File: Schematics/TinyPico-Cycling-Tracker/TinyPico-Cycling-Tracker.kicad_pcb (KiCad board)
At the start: 2 copper layers, 105.2 x 70.1 mm, 17 parts, among them J1 Conn_01x06, J4 Conn_01x06_Socket, SW2 SW_Push, U10 MicroSD Card Adapter, U6 module_mpu6050, U7 SSD1306 0.96" OLED, U8 TinyPico, U9 GPS6MV2

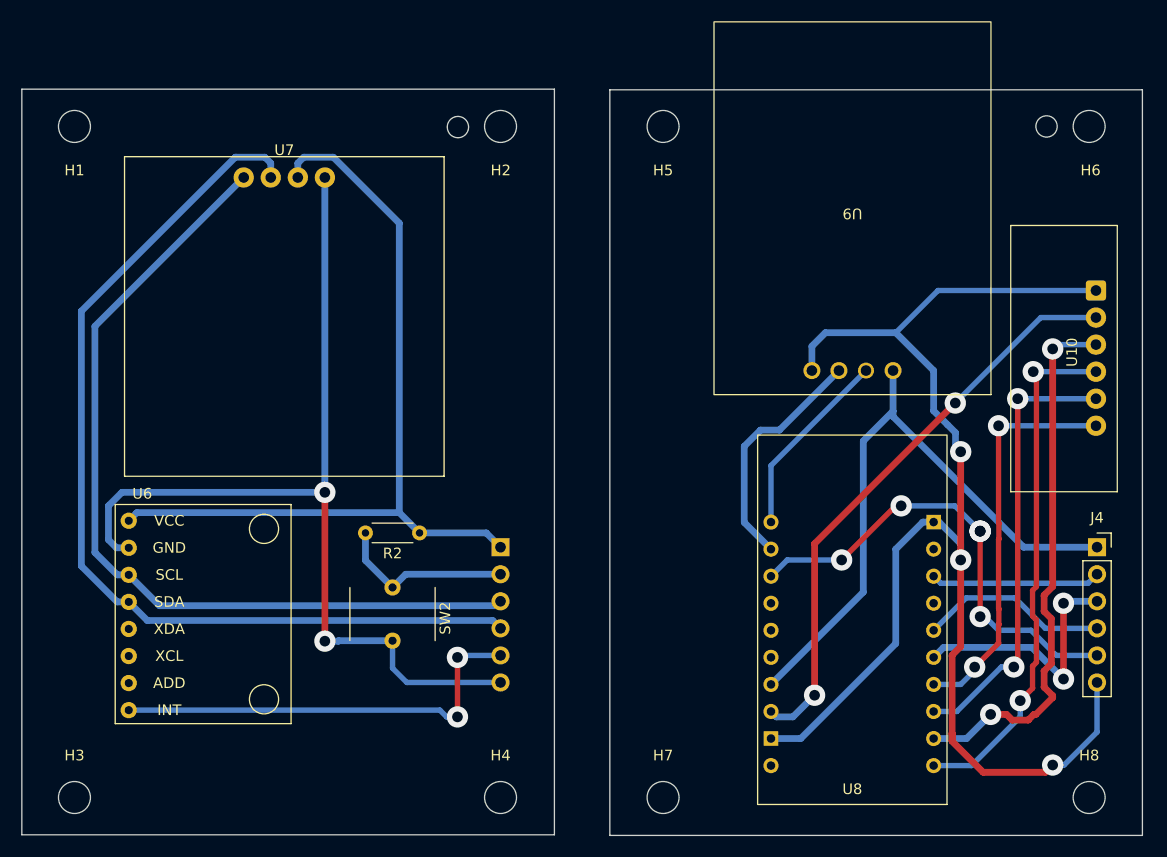
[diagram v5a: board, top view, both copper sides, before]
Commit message: fix: vias warnings
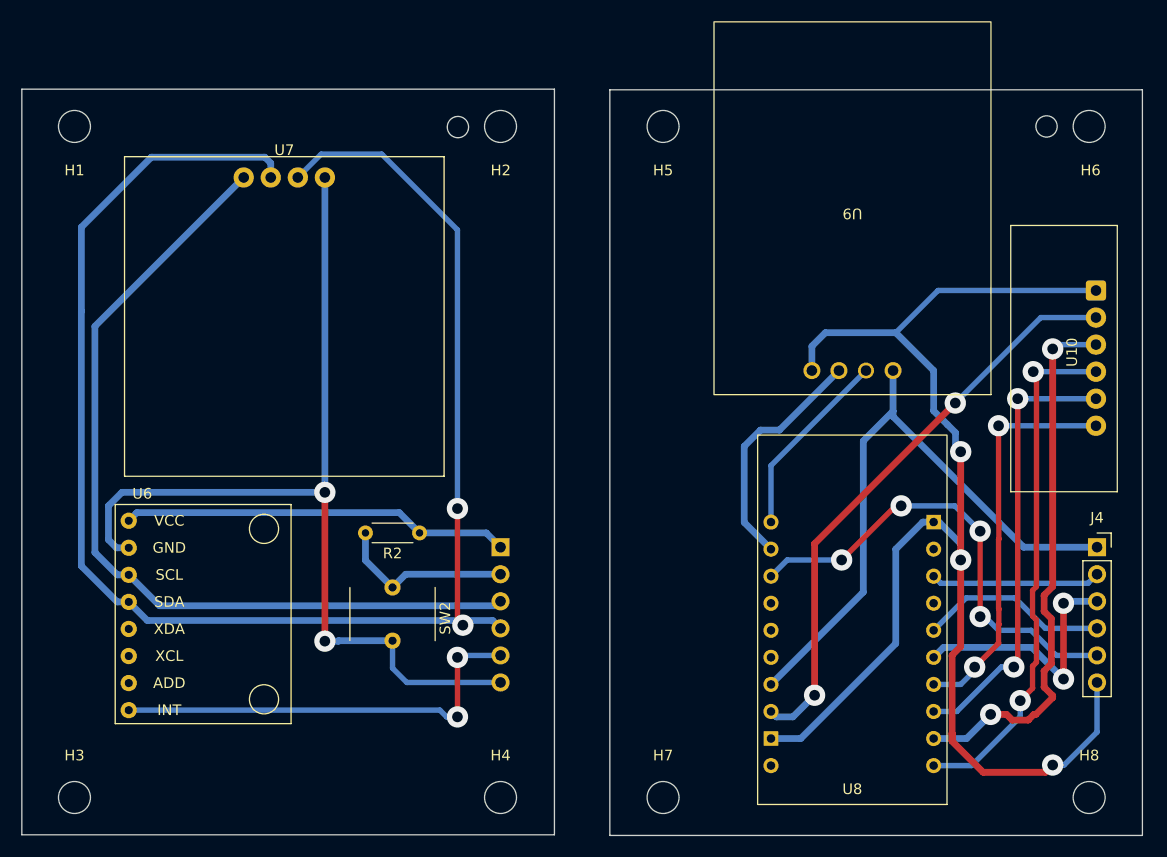
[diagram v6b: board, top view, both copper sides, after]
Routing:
- net /Upper Board/SDA: track 91.1 -> 151.8 mm, vias 0 -> 2
- net VCC1: track 77.4 -> 36.6 mm
- net /Bottom Board/INT: track 45.0 -> 43.9 mm, vias 5 -> 4
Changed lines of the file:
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@@
-	)
-	(segment
-		(start 150.495001 44.582009)
-		(end 150.495001 71.755001)
-		(width 0.635)
-		(layer "B.Cu")
-		(net 7)
 	)
 	(segment
@@
 	)
 	(segment
-		(start 144.299492 38.3865)
-		(end 150.495001 44.582009)
-		(width 0.635)
-		(layer "B.Cu")
-		(net 7)
-	)
-	(segment
-		(start 140.97 38.945462)
-		(end 141.528962 38.3865)
-		(width 0.635)
-		(layer "B.Cu")
-		(net 7)
-	)
-	(segment
 		(start 150.495001 71.755001)
 		(end 152.4 73.66)
@@
 	)
 	(segment
-		(start 140.97 40.2925)
-		(end 140.97 38.945462)
-		(width 0.635)
-		(layer "B.Cu")
-		(net 7)
-	)
-	(segment
 		(start 152.4 73.66)
 		(end 158.66 73.66)
@@
 	)
 	(segment
-		(start 141.528962 38.3865)
-		(end 144.299492 38.3865)
-		(width 0.635)
-		(layer "B.Cu")
-		(net 7)
-	)
-	(segment
 		(start 158.66 73.66)
 		(end 160 75)
@@
 	)
 	(segment
+		(start 155.956 71.374)
+		(end 155.956 81.813)
+		(width 0.508)
+		(layer "F.Cu")
+		(net 8)
+	)
+	(segment
+		(start 155.956 81.813)
+		(end 156.464 82.321)
+		(width 0.508)
+		(layer "F.Cu")
+		(net 8)
+	)
+	(via
+		(at 156.464 82.321)
+		(size 2)
+		(drill 1)
+		(layers "F.Cu" "B.Cu")
+		(net 8)
+	)
+	(via
+		(at 155.956 71.374)
+		(size 2)
+		(drill 1)
+		(layers "F.Cu" "B.Cu")
+		(net 8)
+	)
+	(segment
 		(start 159.2635 81.8835)
 		(end 160 82.62)
@@
 	)
 	(segment
+		(start 120.648 52.839008)
+		(end 120.648 76.76763)
+		(width 0.635)
+		(layer "B.Cu")
+		(net 8)
+	)
+	(segment
 		(start 120.648 76.76763)
 		(end 124.01737 80.137)
@@
 	)
 	(segment
-		(start 135.100508 38.3865)
+		(start 148.844 38.1)
+		(end 155.956 45.212)
+		(width 0.508)
+		(layer "B.Cu")
+		(net 8)
+	)
+	(segment
+		(start 138.43 40.2925)
+		(end 138.43 38.945462)
+		(width 0.635)
+		(layer "B.Cu")
+		(net 8)
+	)
+	(segment
+		(start 120.65 44.958)
+		(end 120.65 52.837008)
+		(width 0.635)
+		(layer "B.Cu")
+		(net 8)
+	)
+	(segment
+		(start 137.871038 38.3865)
+		(end 127.2215 38.3865)
+		(width 0.635)
+		(layer "B.Cu")
+		(net 8)
+	)
+	(segment
+		(start 143.1625 38.1)
+		(end 148.844 38.1)
+		(width 0.508)
+		(layer "B.Cu")
+		(net 8)
+	)
+	(segment
+		(start 120.65 52.837008)
 		(end 120.648 52.839008)
 		(width 0.635)
+		(layer "B.Cu")
+		(net 8)
+	)
+	(segment
+		(start 125.095 80.137)
+		(end 126.8415 81.8835)
+		(width 0.635)
+		(layer "B.Cu")
+		(net 8)
+	)
+	(segment
+		(start 124.01737 80.137)
+		(end 125.095 80.137)
+		(width 0.635)
+		(layer "B.Cu")
+		(net 8)
+	)
+	(segment
+		(start 126.8415 81.8835)
+		(end 159.2635 81.8835)
+		(width 0.635)
+		(layer "B.Cu")
+		(net 8)
+	)
+	(segment
+		(start 127.2215 38.3865)
+		(end 120.65 44.958)
+		(width 0.635)
+		(layer "B.Cu")
+		(net 8)
+	)
+	(segment
+		(start 155.956 45.212)
+		(end 155.956 71.374)
+		(width 0.508)
+		(layer "B.Cu")
+		(net 8)
+	)
+	(segment
+		(start 140.97 40.2925)
+		(end 143.1625 38.1)
+		(width 0.508)
 		(layer "B.Cu")
 		(net 8)
@@
 	)
 	(segment
-		(start 138.43 40.2925)
-		(end 138.43 38.945462)
-		(width 0.635)
-		(layer "B.Cu")
-		(net 8)
-	)
-	(segment
-		(start 120.648 52.839008)
-		(end 120.648 76.76763)
-		(width 0.635)
-		(layer "B.Cu")
-		(net 8)
-	)
-	(segment
-		(start 137.871038 38.3865)
-		(end 135.100508 38.3865)
-		(width 0.635)
-		(layer "B.Cu")
-		(net 8)
-	)
-	(segment
-		(start 125.095 80.137)
-		(end 126.8415 81.8835)
-		(width 0.635)
-		(layer "B.Cu")
-		(net 8)
-	)
-	(segment
-		(start 126.8415 81.8835)
-		(end 159.2635 81.8835)
-		(width 0.635)
-		(layer "B.Cu")
-		(net 8)
-	)
-	(segment
-		(start 124.01737 80.137)
-		(end 125.095 80.137)
-		(width 0.635)
-		(layer "B.Cu")
-		(net 8)
-	)
-	(segment
 		(start 143.51 69.85)
 		(end 143.51 83.82)
@@
 	)
 	(segment
-		(start 205.74 73.66)
-		(end 205.232 73.152)
-		(width 0.508)
-		(layer "F.Cu")
-		(net 28)
-	)
-	(segment
 		(start 197.104 71.12)
 		(end 192.024 76.2)
@@
 	)
 	(segment
-		(start 205.232 73.152)
-		(end 205.025499 73.358501)
+		(start 205.025499 81.517999)
+		(end 205.0255 81.518)
+		(width 0.508)
+		(layer "F.Cu")
+		(net 28)
+	)
+	(segment
+		(start 205.025499 73.495146)
+		(end 205.025499 81.517999)
 		(width 0.508)
 		(layer "F.Cu")
@@
 		(net 28)
 	)
-	(segment
-		(start 205.0255 73.495147)
-		(end 205.025499 73.495146)
-		(width 0.508)
-		(layer "F.Cu")
-		(net 28)
-	)
-	(segment
-		(start 205.0255 81.518)
-		(end 205.0255 73.495147)
-		(width 0.508)
-		(layer "F.Cu")
-		(net 28)
-	)
-	(segment
-		(start 205.025499 73.358501)
-		(end 205.025499 73.495146)
-		(width 0.508)
-		(layer "F.Cu")
-		(net 28)
-	)
 	(via
 		(at 197.612 71.12)
 		(size 2)
 		(drill 1)
-		(layers "F.Cu" "B.Cu")
-		(net 28)
-	)
-	(via
-		(at 205.025499 73.495146)
-		(size 2)
-		(drill 1)
